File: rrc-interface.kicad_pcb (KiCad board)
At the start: 2 copper layers, 169.8 x 127 mm, 52 parts, among them J1 Mic Jack, J10 Input Only Pins, J11 Input Only Pins, J12 Flash mode, J13 Switch Assembly, J15 RRC Optional Config DIP Socket, J2 To RRC, J3 6P6C RRC, J4 Audio Out, J5 Ptt, J6 TF Set, J8 UART Socket, J9 SPI Breakout, U1 ESP32-DevKitC, U3 ADG884xRM

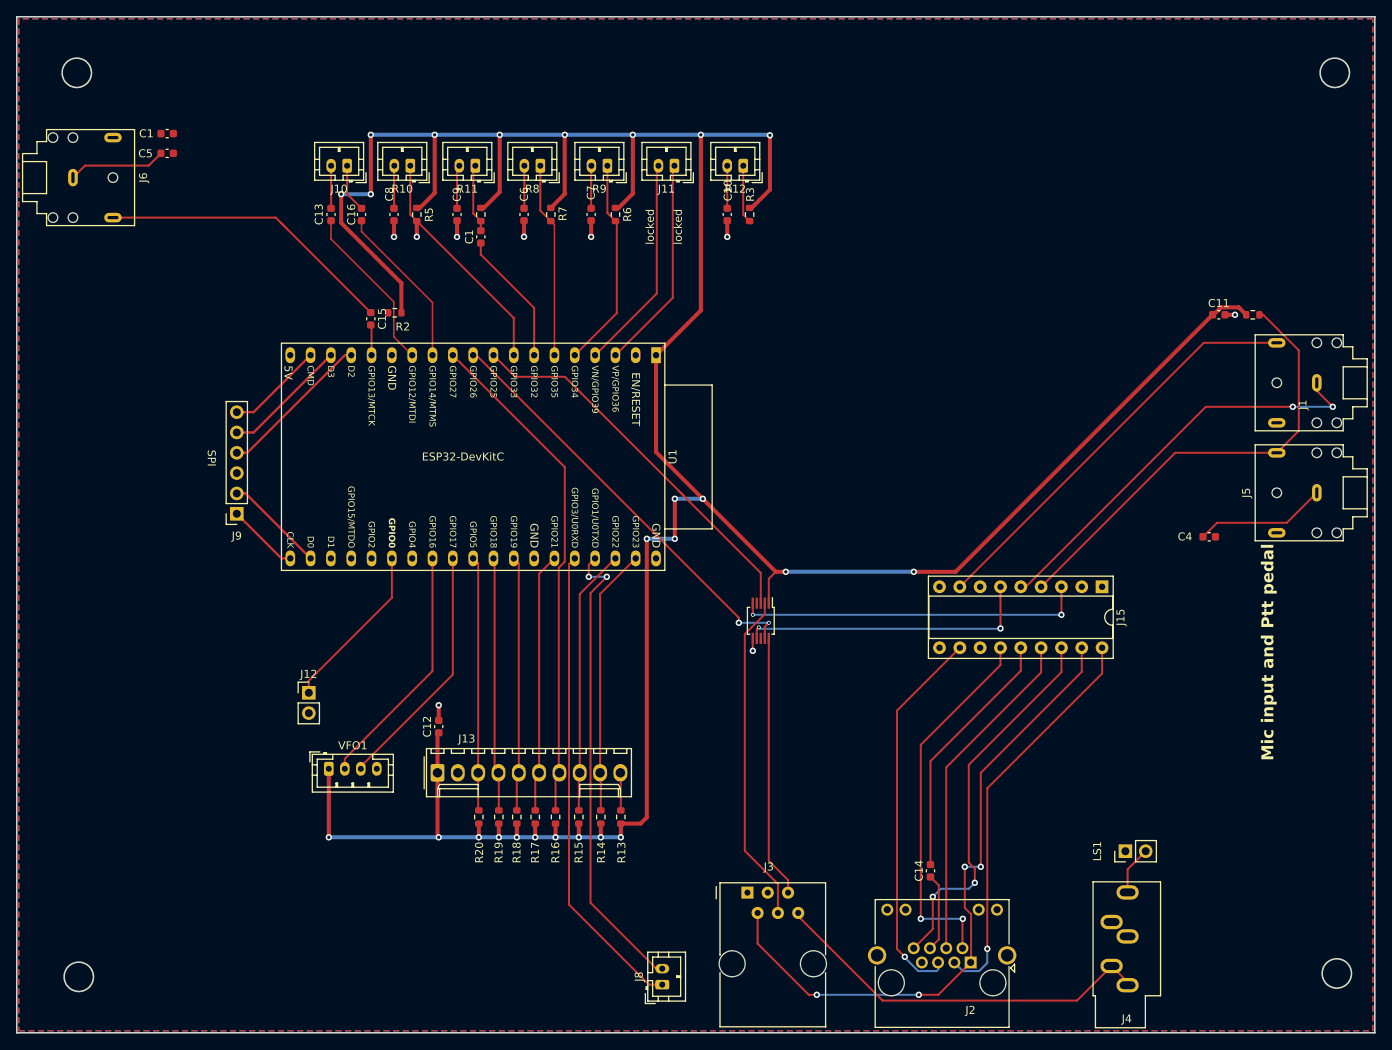
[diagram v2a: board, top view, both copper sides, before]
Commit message: update main board routing, add 3d models and improve layout
Changes:

* update main board layout a bit
* try to improve routing
* add 3d model for 6p6c
* add decoupling caps to ptt line
* almost finish pot board
* switch board almost finished

Details:
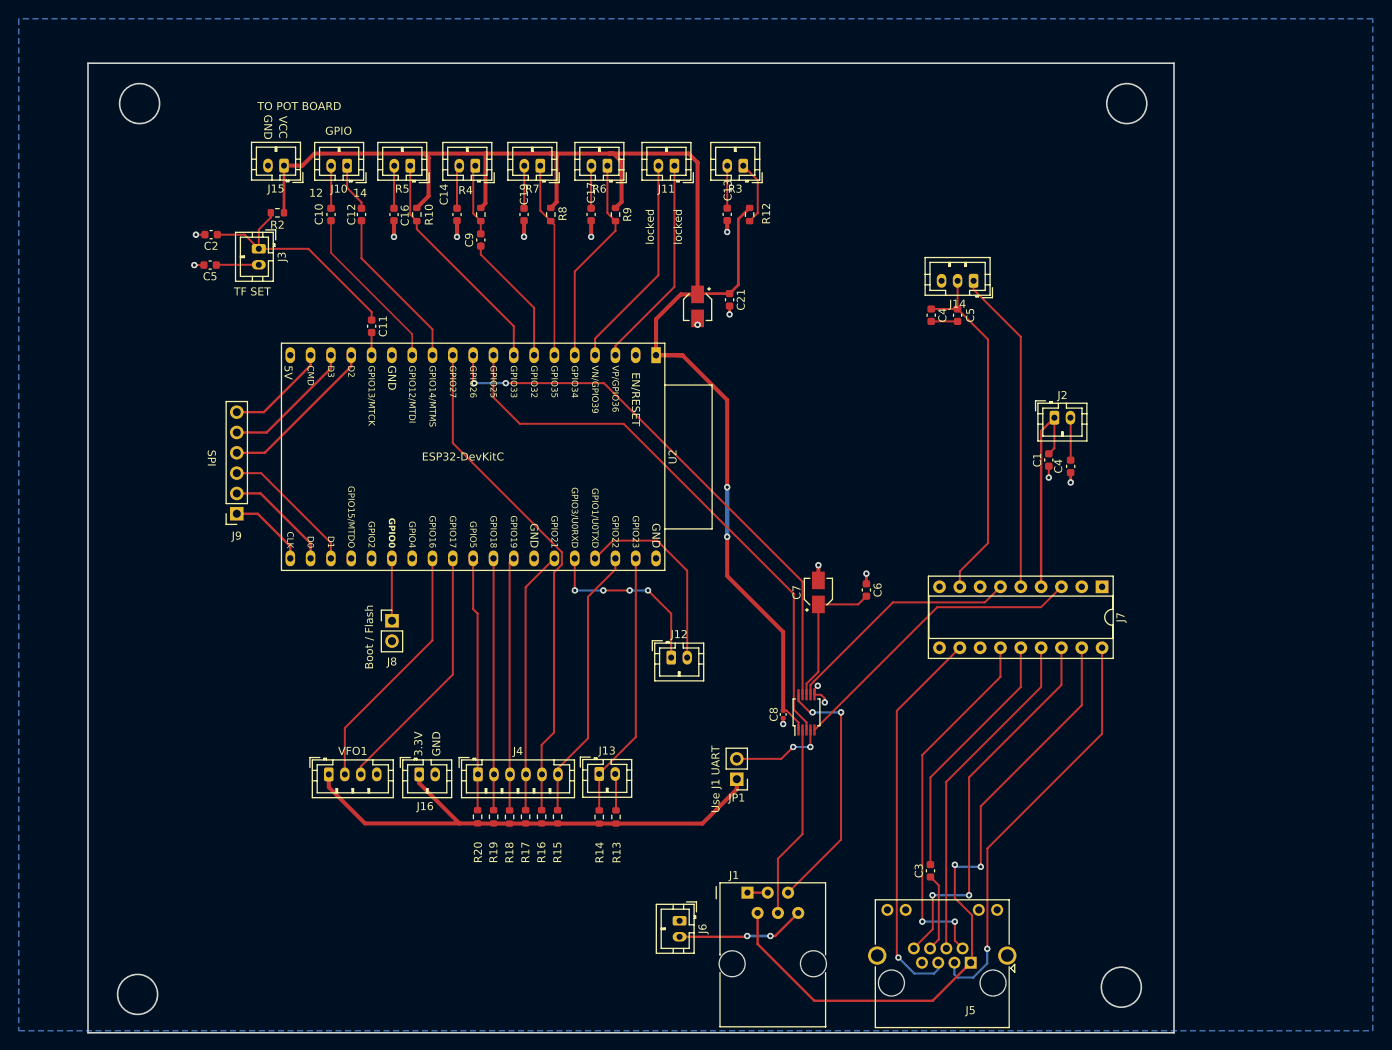
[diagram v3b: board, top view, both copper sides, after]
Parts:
- removed the C11 at (163.0, 50.2)
- removed the C12 at (65.5, 101.7)
- removed the C5 at (31.5, 30.1)
- removed the J1 at (175.2, 58.8)
- removed the J5 at (175.2, 72.5)
- removed LS1: Speaker, Connector_PinHeader_2.54mm:PinHeader_1x02_P2.54mm_Vertical
- removed R1: 2.2K, Resistor_SMD:R_0603_1608Metric
- added C2: 0.1uF, Capacitor_SMD:C_0603_1608Metric, F.Cu at (37.0, 40.2)
- added C20: 10 uF, Capacitor_SMD:CP_Elec_3x5.3, F.Cu at (97.8, 49.2)
- added C21: 0.1uF, Capacitor_SMD:C_0603_1608Metric, F.Cu at (101.8, 48.4)
- added C4: 0.1 uF, Capacitor_SMD:C_0603_1608Metric, F.Cu at (127.0, 50.3)
- added C5: 0.1uF, Capacitor_SMD:C_0603_1608Metric, F.Cu at (36.9, 44.0)
- added C5: 330 pF, Capacitor_SMD:C_0603_1608Metric, F.Cu at (130.3, 50.3)
- added C6: 0.1uF, Capacitor_SMD:C_0603_1608Metric, F.Cu at (119.0, 84.7)
- added C7: 10 uF, Capacitor_SMD:CP_Elec_3x5.3, F.Cu at (113.0, 85.0)
- added C8: 0.1uF, Capacitor_SMD:C_0402_1005Metric, F.Cu at (108.5, 100.2)
- added J14: Mic input, Connector_JST:JST_PH_B3B-PH-K_1x03_P2.00mm_Vertical, F.Cu at (132.3, 46.0)
- added J15: VCC & GND for pot board, Connector_JST:JST_PH_B2B-PH-K_1x02_P2.00mm_Vertical, F.Cu at (46.1, 31.6)
- added J16: 3V & GND, Connector_JST:JST_PH_B2B-PH-K_1x02_P2.00mm_Vertical, F.Cu at (63.0, 107.7)
- added J2: Ptt, Connector_JST:JST_PH_B2B-PH-K_1x02_P2.00mm_Vertical, F.Cu at (142.5, 63.1)
- added J3: TF Set, Connector_JST:JST_PH_B2B-PH-K_1x02_P2.00mm_Vertical, F.Cu at (43.0, 42.0)
- added JP1: Jumper_2_Open, Connector_PinHeader_2.54mm:PinHeader_1x02_P2.54mm_Vertical, F.Cu at (102.8, 108.3)
- J1: renamed from J3; footprint Connector_RJ:RJ12_Amphenol_54601 -> Library:RJ12_Amphenol_54601
- J13: value Switch Assembly -> Conn_01x02; footprint Connector_Molex:Molex_KK-254_AE-6410-10A_1x10_P2.54mm_Vertical -> Connector_JST:JST_PH_B2B-PH-K_1x02_P2.00mm_Vertical
- J4: value Audio Out -> Conn_01x06; footprint Connector_Audio:Jack_3.5mm_CUI_SJ1-3535NG_Horizontal -> Connector_JST:JST_PH_B6B-PH-K_1x06_P2.00mm_Vertical
- J6: value TF Set -> Audio Output; footprint Connector_Audio:Jack_3.5mm_CUI_SJ1-3523N_Horizontal -> Connector_JST:JST_PH_B2B-PH-K_1x02_P2.00mm_Vertical
- moved J6 119.9 mm to (95.6, 126.0)
- moved C1 117.5 mm to (141.8, 68.4), turned to 90 degrees
- moved J4 85.4 mm to (70.4, 107.7), turned to 0 degrees
- moved J12 40.9 mm to (94.5, 93.1), turned to 0 degrees
- moved J13 20.2 mm to (85.5, 107.7)
- moved C4 19.4 mm to (144.5, 69.2), turned to -90 degrees
- moved R2 19.3 mm to (45.3, 37.5)
- moved J8 13.8 mm to (59.6, 88.5)
- moved U1 12.8 mm to (111.5, 99.9), turned to 90 degrees
- moved R15 2.65 mm to (80.3, 113.0)
- moved R16 1.75 mm to (78.3, 113.0)
- moved R17 1.21 mm to (76.3, 113.0)
- moved C11 0.94 mm to (57.1, 51.7)
- moved R18 0.90 mm to (74.3, 113.0)
- moved VFO1 0.70 mm to (51.8, 107.7)
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- renumbered C13 to C10, C15 to C11, C16 to C12, C10 to C13, C9 to C14, C8 to C16, C7 to C17, C6 to C19, C14 to C3, C1 to C9, J8 to J12, J2 to J5, J15 to J7, J12 to J8, R5 to R10, R4 to R11, R3 to R12, R12 to R3, R11 to R4, R10 to R5, R9 to R6, R8 to R7, R7 to R8, R6 to R9, U3 to U1, U1 to U2
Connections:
- C1 pad 2: GND -> PTT
- J13 pad 1: +3V3 -> Band
- J13 pad 2: GND -> On/Off
- R10 pad 1: +3V3 -> +3.3V
- R11 pad 1: +3V3 -> +3.3V
- R12 pad 1: +3V3 -> +3.3V
- R13 pad 1: +3V3 -> +3.3V
- R14 pad 1: +3V3 -> +3.3V
- R15 pad 1: +3V3 -> +3.3V
- R16 pad 1: +3V3 -> +3.3V
- R17 pad 1: +3V3 -> +3.3V
- R18 pad 1: +3V3 -> +3.3V
- R19 pad 1: +3V3 -> +3.3V
- R2 pad 2: +3V3 -> +3.3V
- R20 pad 1: +3V3 -> +3.3V
- R8 pad 1: +3V3 -> +3.3V
- R9 pad 1: +3V3 -> +3.3V
- U1 pad 1: +3V3 -> +3.3V
- U2 pad 1: +3V3 -> +3.3V
- U2 pad 19: +5V -> unconnected-(U2-5V-Pad19)
- VFO1 pad 1: +3V3 -> +3.3V
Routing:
- net +3V3: track 393.7 -> 0.00 mm, vias 25 -> 0
- net +3.3V: track 0.00 -> 258.1 mm, vias 0 -> 2
- net /TX: track 59.4 -> 22.8 mm, vias 0 -> 4
- net /RX: track 58.8 -> 24.9 mm, vias 2 -> 0
- net AF: track 49.0 -> 16.5 mm, vias 0 -> 2
- net PTT: track 99.9 -> 69.1 mm
- net Net-(JP1-B): track 0.00 -> 30.3 mm, vias 0 -> 2
- net /SD_DATA1: track 0.00 -> 17.3 mm
- net GND: track 14.6 -> 30.3 mm, vias 8 -> 16
- net /TDO: track 86.4 -> 100.9 mm, vias 2 -> 4
- net /Boot / Flash: track 21.1 -> 7.81 mm
- net Net-(C5-Pad1): track 12.3 -> 0.00 mm
- net Net-(J2-Pin_2): track 16.5 -> 5.32 mm
- net MIC: track 83.9 -> 73.1 mm, vias 2 -> 0
- net TF Set: track 37.6 -> 29.5 mm
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- removed copper zone on F.Cu, net GND
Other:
- board size 169.8 x 127 mm -> 135.8 x 121.2 mm
- board text removed: "Mic input and Ptt pedal"

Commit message: cont work on boards
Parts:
- removed C19: 0.1uF, Capacitor_SMD:C_0603_1608Metric
- removed the C4 at (144.5, 69.2)
- removed the C4 at (127.0, 50.3)
- removed the C5 at (36.9, 44.0)
- removed the C5 at (130.3, 50.3)
- removed R3, R4, R5, R6, R7: R_Variable, Connector_JST:JST_PH_B2B-PH-K_1x02_P2.00mm_Vertical
- added C15: 0.1uF, Capacitor_SMD:C_0603_1608Metric, F.Cu at (131.3, 39.7)
- added C4: 0.1 uF, Capacitor_SMD:C_0603_1608Metric, F.Cu at (156.2, 79.6)
- added C5: 330 pF, Capacitor_SMD:C_0603_1608Metric, F.Cu at (156.2, 82.7)
- added J17: RF Gain, Connector_JST:JST_PH_B3B-PH-K_1x03_P2.00mm_Vertical, F.Cu at (72.3, 32.4)
- added J18: AF Gain, Connector_JST:JST_PH_B3B-PH-K_1x03_P2.00mm_Vertical, F.Cu at (63.0, 32.4)
- added J19: IF Shift, Connector_JST:JST_PH_B3B-PH-K_1x03_P2.00mm_Vertical, F.Cu at (91.1, 32.4)
- added J20: Spare, Connector_JST:JST_PH_B3B-PH-K_1x03_P2.00mm_Vertical, F.Cu at (100.5, 32.4)
- added J21: Passthrough, Connector_RJ:RJ45_Amphenol_RJHSE538X, F.Cu at (126.2, 27.6)
- J15: value VCC & GND for pot board -> Rit Xit Value; footprint Connector_JST:JST_PH_B2B-PH-K_1x02_P2.00mm_Vertical -> Connector_JST:JST_PH_B3B-PH-K_1x03_P2.00mm_Vertical
- moved J14 48.4 mm to (161.5, 84.7), turned to 90 degrees
- moved J15 35.6 mm to (81.8, 32.4)
- moved U1 24.7 mm to (110.3, 75.2)
- moved C6 24.4 mm to (111.0, 61.6), turned to 180 degrees
- moved J2 22.5 mm to (161.5, 75.0), turned to 90 degrees
- moved C8 21.3 mm to (107.7, 78.9)
- moved C20 20.6 mm to (107.7, 31.1), turned to 0 degrees
- moved C7 18.8 mm to (112.0, 66.2), turned to 0 degrees
- moved J11 18.1 mm to (89.6, 48.9)
- moved C1 16.9 mm to (157.2, 75.3), turned to 0 degrees
- moved J12 14.7 mm to (93.4, 107.7)
- moved C21 12.5 mm to (106.9, 37.0), turned to 0 degrees
- moved JP1 7.41 mm to (100.5, 101.2), turned to 90 degrees
- moved C13 6.22 mm to (95.5, 36.4)
- moved R12 5.98 mm to (98.5, 36.4), turned to 90 degrees
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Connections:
- C13 pad 1: Net-(C13-Pad1) -> /Spare
- C14 pad 1: Net-(C14-Pad1) -> /RF Gain
- C16 pad 1: Net-(C16-Pad1) -> /AF Gain
- C17 pad 1: Net-(C17-Pad1) -> /IF Shift
- J15 pad 2: GND -> /Rit/Xit Value
- U2 pad 19: unconnected-(U2-5V-Pad19) -> +5V
- VFO1 pad 1: +3.3V -> +5V
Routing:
- net PWR 8V: track 84.5 -> 165.8 mm, vias 2 -> 3
- net SPK OUT: track 51.9 -> 126.3 mm, vias 1 -> 2
- net +5V: track 0.00 -> 69.1 mm
- net PTT: track 69.1 -> 133.9 mm, vias 0 -> 4
- net MICE: track 92.9 -> 155.4 mm, vias 1 -> 2
- net TXD: track 76.9 -> 138.0 mm
- net RXD: track 86.2 -> 146.8 mm, vias 2 -> 4
- net MIC: track 73.1 -> 105.2 mm
- net /GPIO 39: track 27.0 -> 7.48 mm
- net /GPIO 36: track 26.7 -> 7.26 mm
- net /RX: track 24.9 -> 41.4 mm
- net /TX: track 22.8 -> 35.4 mm
- net +3.3V: track 258.1 -> 270.2 mm
- net Net-(JP1-B): track 30.3 -> 41.9 mm
- net Net-(C15-Pad1): track 0.00 -> 9.64 mm
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- added copper zone on F.Cu, net GND
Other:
- board size 135.8 x 121.2 mm -> 148.2 x 121.2 mm
- board text added: "J1 OR J5 SELECT"
- board text added: "Mic input"
- board text added: "Passtrough"
- board text added: "RRC Input"
